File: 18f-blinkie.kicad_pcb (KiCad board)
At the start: 2 copper layers, 69.8 x 61.2 mm, 16 parts, among them J1 Conn_01x07_Female, J2 Conn_01x07_Female

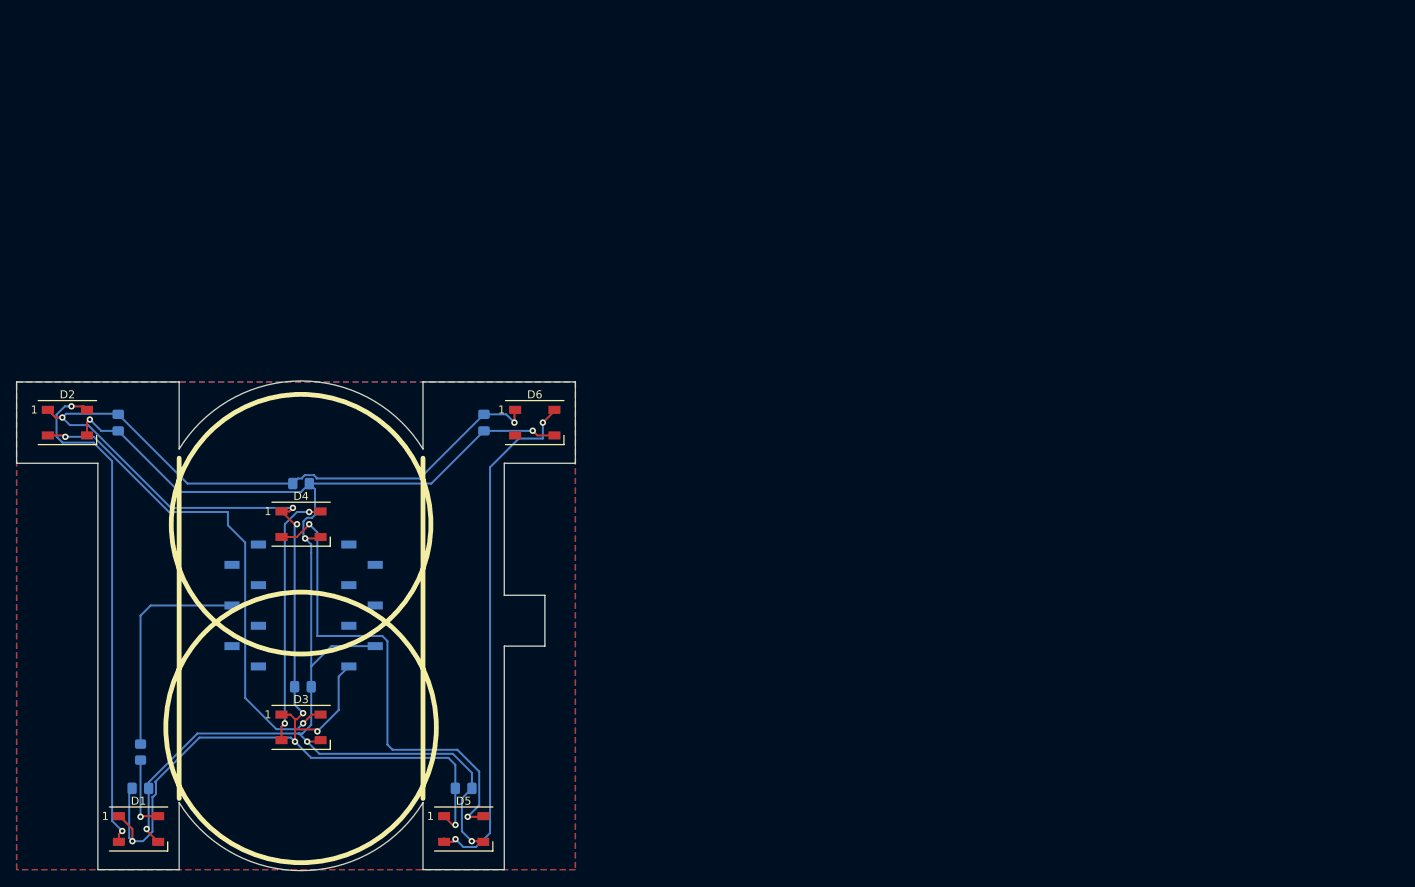
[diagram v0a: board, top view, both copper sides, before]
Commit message: Resized and retraced.
The board was smaller than it had to be; why/how I did that, I do not know.

Now, the board is close to the max dimension for low-cost fab. Wiring is
neater, because I knew what I was doing. So, power/ground route around
the edges (largely), and then I routed data.

It is still the case that all vias are drilled *under* the LEDs, which
maintains the appearance of the board.

I probably should move the header up (to create more space for the USB
cable), but... that would be a lot of re-routing at this point. And,
it might not be an issue.

SO. I will give it one more look, but will probably send this version off
for fab as "v2".
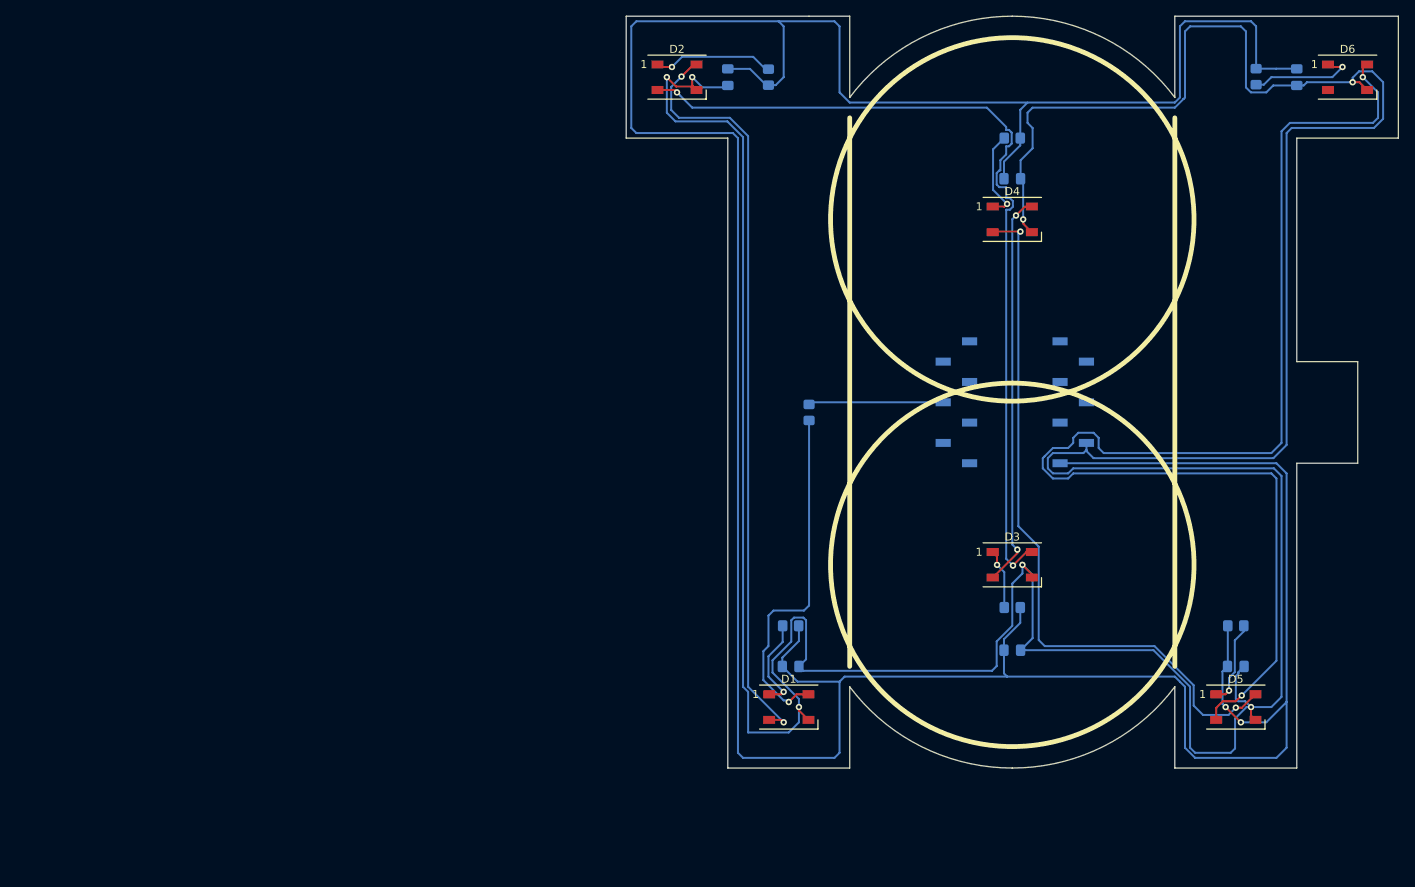
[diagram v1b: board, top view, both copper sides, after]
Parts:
- removed REF**: OSHW-Logo2_14.6x12mm_SilkScreen, Symbol:OSHW-Logo2_14.6x12mm_SilkScreen
- added R0: 220, Resistor_SMD:R_0805_2012Metric_Pad1.20x1.40mm_HandSolder, B.Cu at (152.4, 100.3)
- added R2: 220R, Resistor_SMD:R_0805_2012Metric_Pad1.20x1.40mm_HandSolder, B.Cu at (147.3, 58.4)
- added R3: 220R, Resistor_SMD:R_0805_2012Metric_Pad1.20x1.40mm_HandSolder, B.Cu at (177.8, 124.7)
- added R4: 220R, Resistor_SMD:R_0805_2012Metric_Pad1.20x1.40mm_HandSolder, B.Cu at (177.8, 66.0)
- added R5: 220R, Resistor_SMD:R_0805_2012Metric_Pad1.20x1.40mm_HandSolder, B.Cu at (205.7, 127.0)
- added R6: 220R, Resistor_SMD:R_0805_2012Metric_Pad1.20x1.40mm_HandSolder, B.Cu at (208.3, 58.4)
- R1: value 220 -> 220R
- moved C6 110.4 mm to (213.4, 58.4)
- moved D6 110.4 mm to (219.7, 58.4)
- moved C5 97.7 mm to (205.7, 132.1)
- moved D5 97.7 mm to (205.7, 137.2)
- moved C4 96.7 mm to (177.8, 71.1)
- moved D4 96.7 mm to (177.8, 76.2)
- moved J1 92.5 mm to (170.8, 99.1)
- moved J2 92.5 mm to (185.4, 99.1)
- moved D3 91.2 mm to (177.8, 119.4)
- moved C3 88.8 mm to (177.8, 130.0)
- moved C2 87.6 mm to (142.2, 58.4)
- moved D2 87.6 mm to (135.9, 58.4)
- moved R1 82.8 mm to (150.1, 127.0), turned to 0 degrees
- moved D1 82.7 mm to (149.9, 137.2)
- moved C1 82.7 mm to (150.1, 132.1)
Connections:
- D1 pad 1: 5V -> Net-(D1-Pad1)
- D2 pad 1: 5V -> Net-(D2-Pad1)
- D3 pad 1: 5V -> Net-(D3-Pad1)
- D4 pad 1: 5V -> Net-(D4-Pad1)
- D5 pad 1: 5V -> Net-(D5-Pad1)
- D6 pad 1: 5V -> Net-(D6-Pad1)
- R1 pad 1: DATA -> Net-(D1-Pad1)
- R1 pad 2: Net-(J1-Pad4) -> 5V
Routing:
- net GND: track 178.1 -> 472.8 mm, vias 6 -> 7
- net 5V: track 220.2 -> 431.4 mm, vias 9 -> 2
- net Net-(D5-Pad2): track 65.4 -> 159.5 mm
- net Net-(D2-Pad2): track 62.4 -> 107.5 mm
- net DATA: track 9.32 -> 44.2 mm
- net Net-(D1-Pad2): track 63.6 -> 95.3 mm
- net Net-(D4-Pad2): track 61.6 -> 89.2 mm
- net Net-(D3-Pad2): track 32.3 -> 49.4 mm
- net Net-(D2-Pad1): track 0.00 -> 15.2 mm, vias 0 -> 1
- net Net-(D6-Pad1): track 0.00 -> 13.8 mm, vias 0 -> 1
- net Net-(D1-Pad1): track 0.00 -> 11.7 mm, vias 0 -> 1
- net Net-(D4-Pad1): track 0.00 -> 11.5 mm, vias 0 -> 1
- net Net-(J1-Pad4): track 28.0 -> 16.9 mm
- net Net-(D5-Pad1): track 0.00 -> 10.7 mm, vias 0 -> 1
- net Net-(D3-Pad1): track 0.00 -> 7.53 mm, vias 0 -> 1
- removed copper zone on B.Cu, net (none)
- removed copper zone on F.Cu, net (none)
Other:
- board size 69.8 x 61.2 mm -> 96.5 x 94 mm
